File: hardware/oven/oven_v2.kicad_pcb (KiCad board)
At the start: 2 copper layers, 54.6 x 108 mm, 21 parts, among them J1 NEUTRAL, J10 SERIAL, J2 5V_IN, J3 RELAY_PWR, J4 LIVE, J5 OUTPUT, J6 RELAY_CTRL, J7 DISPLAY, J8 NUMPAD, J9 AVR-ISP-6, U1 ATmega328-AU, U2 MAX6675, Y1 16M

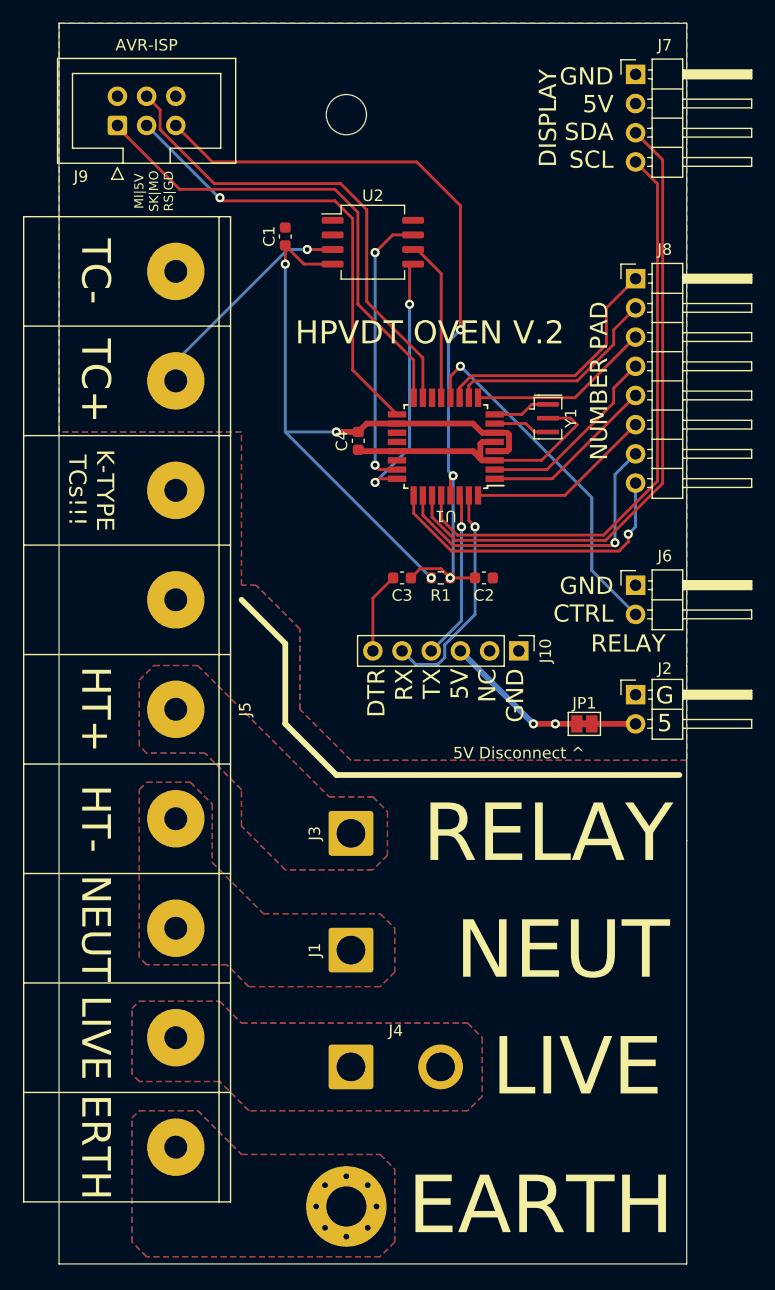
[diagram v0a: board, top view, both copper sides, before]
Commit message: Updated oven revision to have buzzer
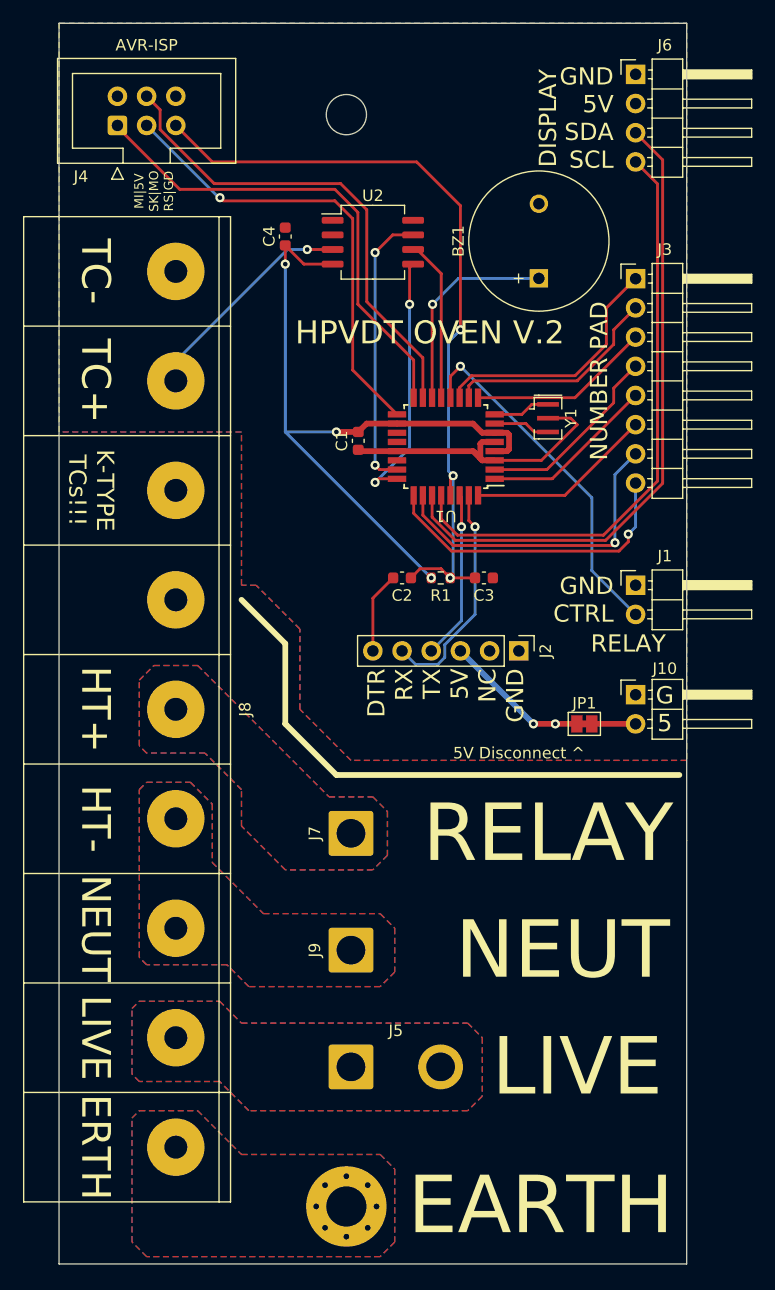
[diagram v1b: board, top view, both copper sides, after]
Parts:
- added BZ1: AT1224TWT, Buzzer_Beeper:MagneticBuzzer_ProSignal_ABT-410-RC, F.Cu at (96.4, 76.8)
- renumbered C4 to C1, C3 to C2, C2 to C3, C1 to C4, J6 to J1, J2 to J10, J10 to J2, J8 to J3, J9 to J4, J4 to J5, J7 to J6, J3 to J7, J5 to J8, J1 to J9
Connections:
- U1 pad 14: unconnected-(U1-Pad14) -> /BUZZ
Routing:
- net /BUZZ: track 0.00 -> 18.3 mm, vias 0 -> 1
